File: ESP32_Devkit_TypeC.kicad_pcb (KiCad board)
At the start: 2 copper layers, 20.3 x 54.4 mm, 62 parts, among them J1 USB_C_Receptacle_USB2.0, J2 Conn_01x19, J3 Conn_01x19, Q1 MMBT3904, Q2 MMBT3904, SW1 EN, SW2 BOOT, U1 SD8942, U2 CH340C, U3 W25Q128JVS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

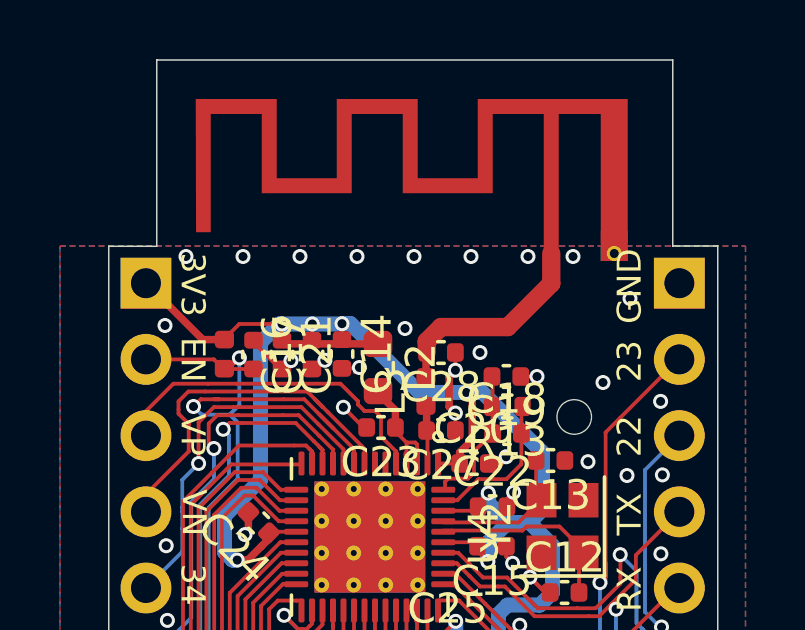
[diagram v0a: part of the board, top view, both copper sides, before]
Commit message: Better RF grounding around antenna connection
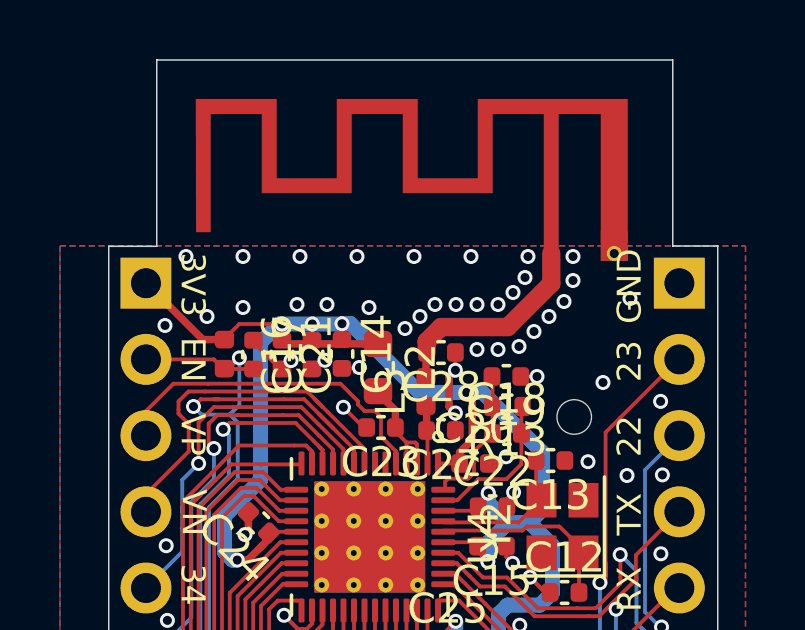
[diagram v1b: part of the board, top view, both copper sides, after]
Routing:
- net GND: vias 86 -> 104
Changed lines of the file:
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@@
   (via (at 108.375 95.87) (size 0.5) (drill 0.3) (layers "F.Cu" "B.Cu") (free) (net 3))
   (via (at 94.416 108.623) (size 0.5) (drill 0.3) (layers "F.Cu" "B.Cu") (net 3))
+  (via (at 94.675 77.95) (size 0.5) (drill 0.3) (layers "F.Cu" "B.Cu") (free) (net 3))
+  (via (at 101.775 77.85) (size 0.5) (drill 0.3) (layers "F.Cu" "B.Cu") (free) (net 3))
   (via (at 98.075 96.85) (size 0.5) (drill 0.3) (layers "F.Cu" "B.Cu") (free) (net 3))
   (via (at 108.475 118.84) (size 0.5) (drill 0.3) (layers "F.Cu" "B.Cu") (free) (net 3))
@@
   (via (at 104.493 99.442) (size 0.5) (drill 0.3) (layers "F.Cu" "B.Cu") (net 3))
   (via (at 102.275 76.25) (size 0.5) (drill 0.3) (layers "F.Cu" "B.Cu") (free) (net 3))
+  (via (at 104.075 76.95) (size 0.5) (drill 0.3) (layers "F.Cu" "B.Cu") (free) (net 3))
+  (via (at 103.175 77.85) (size 0.5) (drill 0.3) (layers "F.Cu" "B.Cu") (free) (net 3))
+  (via (at 102.475 77.85) (size 0.5) (drill 0.3) (layers "F.Cu" "B.Cu") (free) (net 3))
   (via (at 108.435 113.7) (size 0.5) (drill 0.3) (layers "F.Cu" "B.Cu") (free) (net 3))
   (via (at 105.675 76.25) (size 0.5) (drill 0.3) (layers "F.Cu" "B.Cu") (free) (net 3))
@@
   (via (at 96.523 116.87) (size 0.5) (drill 0.3) (layers "F.Cu" "B.Cu") (net 3))
   (via (at 106.704 116.344) (size 0.5) (drill 0.3) (layers "F.Cu" "B.Cu") (net 3))
+  (via (at 103.175 79.35) (size 0.5) (drill 0.3) (layers "F.Cu" "B.Cu") (free) (net 3))
   (via (at 101.755 80.041) (size 0.5) (drill 0.3) (layers "F.Cu" "B.Cu") (net 3))
   (via (at 93.885 107.97) (size 0.5) (drill 0.3) (layers "F.Cu" "B.Cu") (free) (net 3))
+  (via (at 100.575 78.25) (size 0.5) (drill 0.3) (layers "F.Cu" "B.Cu") (free) (net 3))
   (via (at 95.075 114.4) (size 0.5) (drill 0.3) (layers "F.Cu" "B.Cu") (net 3))
   (via (at 108.515 121.37) (size 0.5) (drill 0.3) (layers "F.Cu" "B.Cu") (free) (net 3))
@@
   (via (at 92.045 106.31) (size 0.5) (drill 0.3) (layers "F.Cu" "B.Cu") (free) (net 3))
   (via (at 108.655 103.71) (size 0.5) (drill 0.3) (layers "F.Cu" "B.Cu") (free) (net 3))
+  (via (at 93.475 78.25) (size 0.5) (drill 0.3) (layers "F.Cu" "B.Cu") (free) (net 3))
   (via (at 107.475 83.55) (size 0.5) (drill 0.3) (layers "F.Cu" "B.Cu") (free) (net 3))
   (via (at 102.49 89.15) (size 0.5) (drill 0.3) (layers "F.Cu" "B.Cu") (net 3))
@@
   (via (at 104.175 76.25) (size 0.5) (drill 0.3) (layers "F.Cu" "B.Cu") (free) (net 3))
   (via (at 97.405 79.71) (size 0.5) (drill 0.3) (layers "F.Cu" "B.Cu") (net 3))
+  (via (at 103.875 79.25) (size 0.5) (drill 0.3) (layers "F.Cu" "B.Cu") (free) (net 3))
   (via (at 104.825 90.584) (size 0.5) (drill 0.3) (layers "F.Cu" "B.Cu") (net 3))
   (via (at 106.175 83.09) (size 0.5) (drill 0.3) (layers "F.Cu" "B.Cu") (free) (net 3))
@@
   (via (at 91.995 98.68) (size 0.5) (drill 0.3) (layers "F.Cu" "B.Cu") (free) (net 3))
   (via (at 108.655 83.53) (size 0.5) (drill 0.3) (layers "F.Cu" "B.Cu") (free) (net 3))
+  (via (at 97.475 77.85) (size 0.5) (drill 0.3) (layers "F.Cu" "B.Cu") (free) (net 3))
   (via (at 103.662 86.475) (size 0.5) (drill 0.3) (layers "F.Cu" "B.Cu") (net 3))
+  (via (at 96.475 77.85) (size 0.5) (drill 0.3) (layers "F.Cu" "B.Cu") (free) (net 3))
   (via (at 92.185 118.83) (size 0.5) (drill 0.3) (layers "F.Cu" "B.Cu") (free) (net 3))
   (via (at 102.456 90.834) (size 0.5) (drill 0.3) (layers "F.Cu" "B.Cu") (free) (net 3))
@@
   (via (at 106.675 80.45) (size 0.5) (drill 0.3) (layers "F.Cu" "B.Cu") (free) (net 3))
   (via (at 100.075 78.65) (size 0.5) (drill 0.3) (layers "F.Cu" "B.Cu") (free) (net 3))
+  (via (at 98.875 77.95) (size 0.5) (drill 0.3) (layers "F.Cu" "B.Cu") (free) (net 3))
   (via (at 94.675 76.25) (size 0.5) (drill 0.3) (layers "F.Cu" "B.Cu") (free) (net 3))
+  (via (at 104.875 78.25) (size 0.5) (drill 0.3) (layers "F.Cu" "B.Cu") (free) (net 3))
   (via (at 92.135 90.94) (size 0.5) (drill 0.3) (layers "F.Cu" "B.Cu") (free) (net 3))
   (via (at 104.475 80.249999) (size 0.5) (drill 0.3) (layers "F.Cu" "B.Cu") (net 3))
@@
   (via (at 96.275 79.72) (size 0.5) (drill 0.3) (layers "F.Cu" "B.Cu") (net 3))
   (via (at 103.694 84.108) (size 0.5) (drill 0.3) (layers "F.Cu" "B.Cu") (net 3))
+  (via (at 104.375 78.75) (size 0.5) (drill 0.3) (layers "F.Cu" "B.Cu") (free) (net 3))
   (via (at 104.15 91.823) (size 0.5) (drill 0.3) (layers "F.Cu" "B.Cu") (net 3))
   (via (at 107.575 77.65) (size 0.5) (drill 0.3) (layers "F.Cu" "B.Cu") (free) (net 3))
   (via (at 102.974 103.254) (size 0.5) (drill 0.3) (layers "F.Cu" "B.Cu") (net 3))
   (via (at 92.025 103.79) (size 0.5) (drill 0.3) (layers "F.Cu" "B.Cu") (free) (net 3))
+  (via (at 103.675 77.45) (size 0.5) (drill 0.3) (layers "F.Cu" "B.Cu") (free) (net 3))
   (via (at 92.775 76.25) (size 0.5) (drill 0.3) (layers "F.Cu" "B.Cu") (free) (net 3))
   (via (at 100.219999 102.297501) (size 0.5) (drill 0.3) (layers "F.Cu" "B.Cu") (net 3))
   (via (at 94.733 118.245) (size 0.5) (drill 0.3) (layers "F.Cu" "B.Cu") (net 3))
+  (via (at 105.675 77.05) (size 0.5) (drill 0.3) (layers "F.Cu" "B.Cu") (free) (net 3))
   (via (at 101.495 93.15) (size 0.5) (drill 0.3) (layers "F.Cu" "B.Cu") (free) (net 3))
   (via (at 108.325 100.91) (size 0.5) (drill 0.3) (layers "F.Cu" "B.Cu") (free) (net 3))
@@
   (via (at 103.448 82.925) (size 0.5) (drill 0.3) (layers "F.Cu" "B.Cu") (net 3))
   (via (at 92.115 85.89) (size 0.5) (drill 0.3) (layers "F.Cu" "B.Cu") (free) (net 3))
-  (via (at 102.575 79.45) (size 0.5) (drill 0.3) (layers "F.Cu" "B.Cu") (free) (net 3))
+  (via (at 102.475 79.35) (size 0.5) (drill 0.3) (layers "F.Cu" "B.Cu") (free) (net 3))
   (via (at 104.241 86.939) (size 0.5) (drill 0.3) (layers "F.Cu" "B.Cu") (net 3))
   (via (at 105.55 116.401) (size 0.5) (drill 0.3) (layers "F.Cu" "B.Cu") (net 3))
+  (via (at 105.375 77.75) (size 0.5) (drill 0.3) (layers "F.Cu" "B.Cu") (free) (net 3))
   (via (at 98.021187 81.275705) (size 0.5) (drill 0.3) (layers "F.Cu" "B.Cu") (net 3))
   (via (at 99.445 111.469) (size 0.5) (drill 0.3) (layers "F.Cu" "B.Cu") (net 3))
+  (via (at 101.075 77.85) (size 0.5) (drill 0.3) (layers "F.Cu" "B.Cu") (free) (net 3))
   (via (at 99.555 101.4425) (size 0.5) (drill 0.3) (layers "F.Cu" "B.Cu") (net 3))
   (segment (start 109.22 92.38) (end 107.415 90.575) (width 0.25) (layer "B.Cu") (net 3))

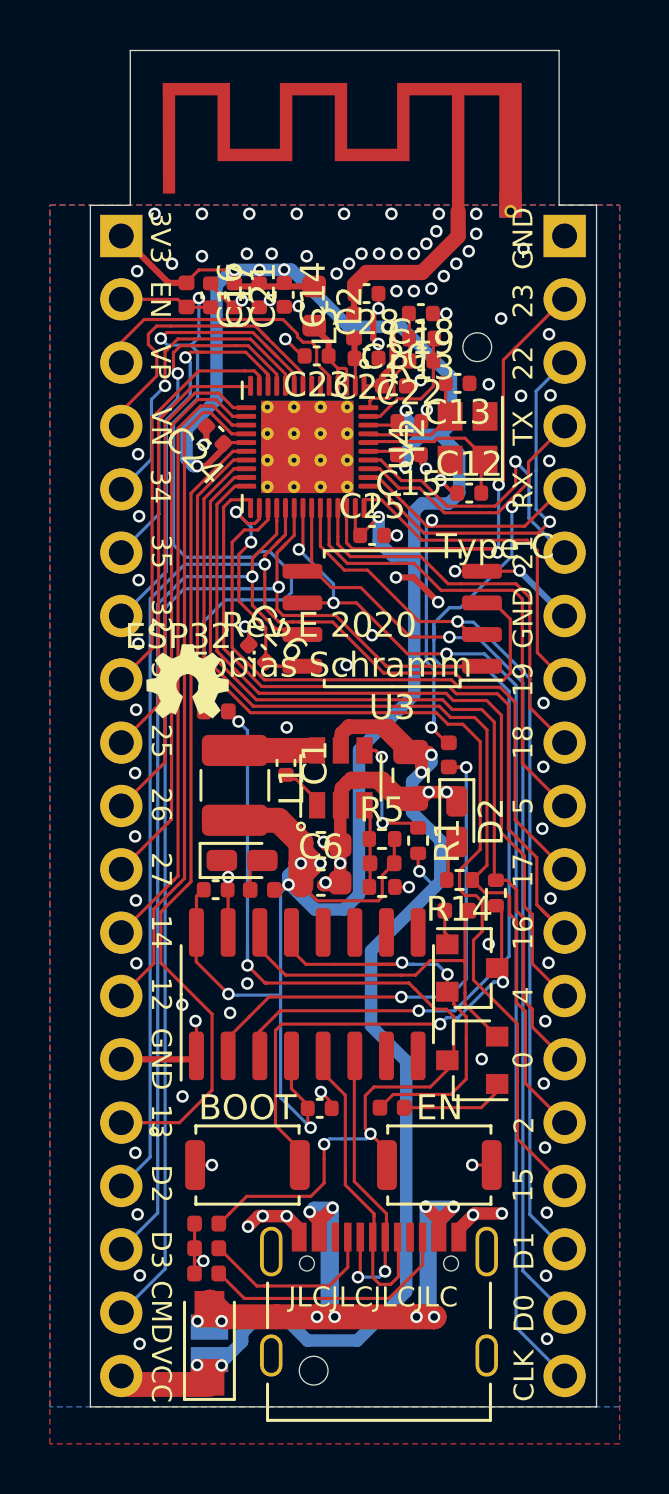
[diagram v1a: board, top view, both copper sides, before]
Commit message: Setup silkscreen
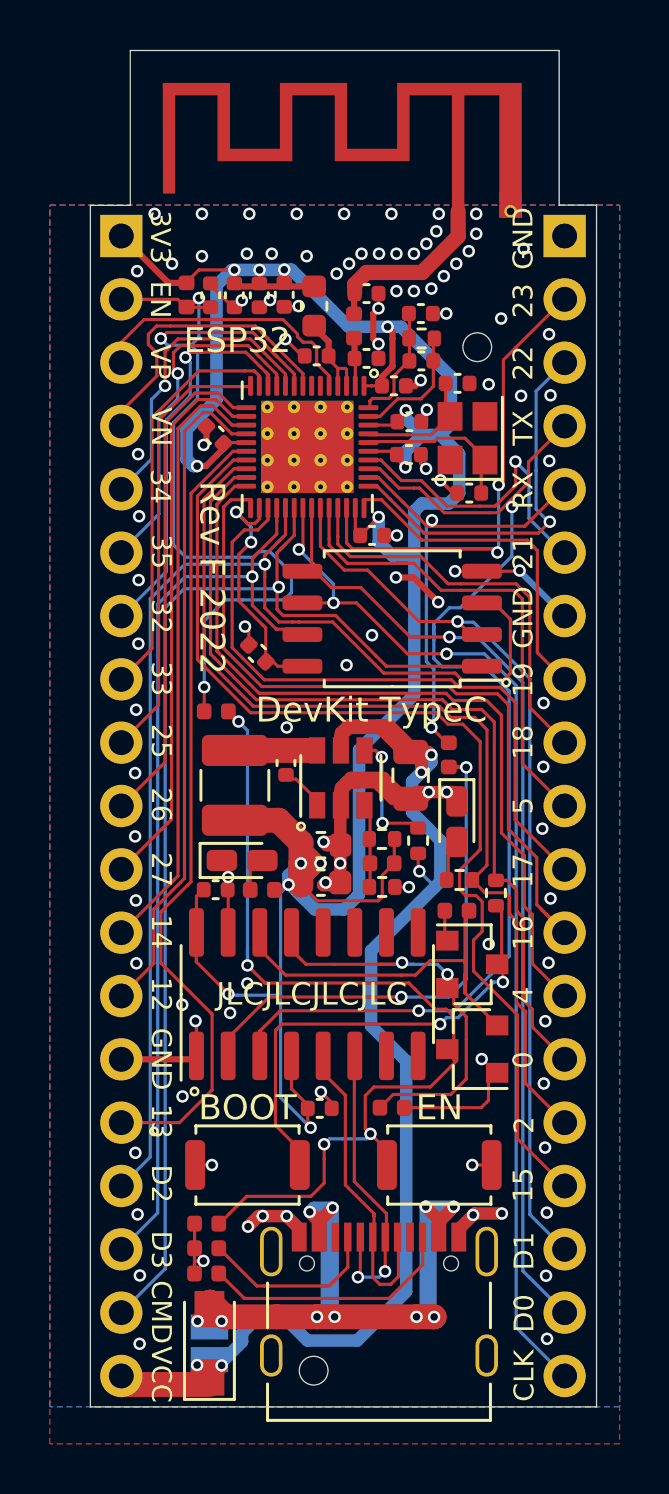
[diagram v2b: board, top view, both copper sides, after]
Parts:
- removed I2: Icon, Signs:OSHW_icon_3.3x3
- moved Q1 0.45 mm to (105.5, 109.8)
- moved Q2 0.15 mm to (105.5, 106.3)
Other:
- board text added: "Designed by Tobias Schramm in 2022"
- board text added: "DevKit TypeC"
- board text added: "Rev F 2022"
- board text removed: "Rev E 2020"
- board text removed: "Tobias Schramm"
- board text removed: "Type C"

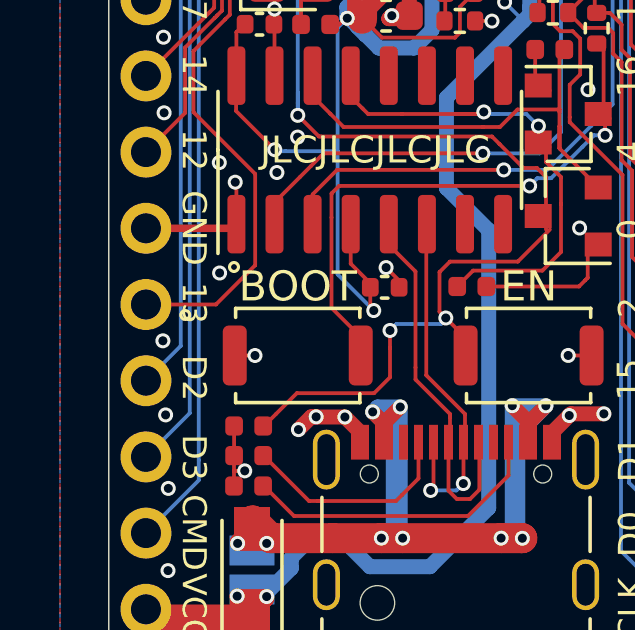
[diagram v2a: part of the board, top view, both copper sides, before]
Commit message: Remove stray pin1 dot
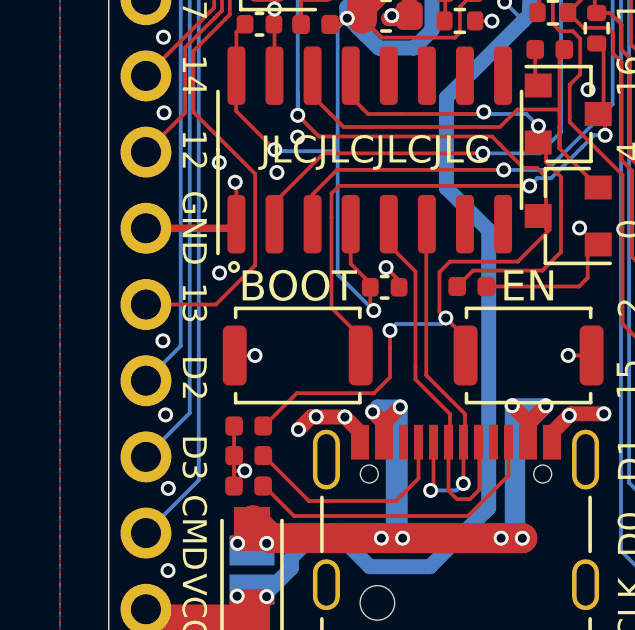
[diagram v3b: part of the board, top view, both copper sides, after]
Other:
- rule pad_to_mask_clearance: 0.01 -> 0
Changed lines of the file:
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@@
       (dielectric_constraints no)
     )
-    (pad_to_mask_clearance 0.01)
+    (pad_to_mask_clearance 0)
     (pad_to_paste_clearance_ratio -0.12)
     (grid_origin 102.075 86.75)
@@
       (drillshape 0)
       (scaleselection 1)
-      (outputdirectory "")
+      (outputdirectory "fab")
     )
   )
@@
       (net 4 "VCC") (pinfunction "B") (pintype "passive"))
   )
-  (gr_circle (center 92.75 113.05) (end 92.8 113.05) (layer "F.SilkS") (width 0.3) (fill none))
   (gr_circle (center 101.575 82.65) (end 101.625 82.65) (layer "F.SilkS") (width 0.3) (fill none))
   (gr_circle (center 98.645 100.8225) (end 98.695 100.8225) (layer "F.SilkS") (width 0.3) (fill none))
